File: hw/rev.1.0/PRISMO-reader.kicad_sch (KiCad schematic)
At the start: 48 parts, among them J1 Conn_01x03, J3 PN532 Connector, J4 External 5V power, J5 USB4120-03-C_REVA, K1 G5LE-1, Q1 2N7002, Q2 BC847, Q3 BC847, SW1 Logout button, U1 ESP32-WROOM-32D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

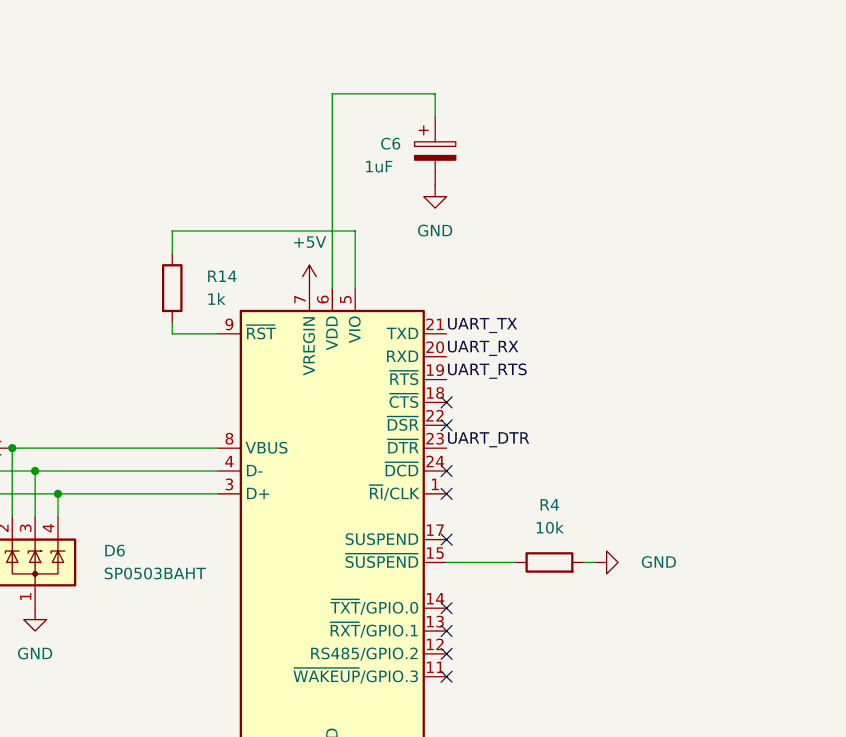
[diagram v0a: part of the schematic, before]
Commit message: fixed CP2102 peripheral connection
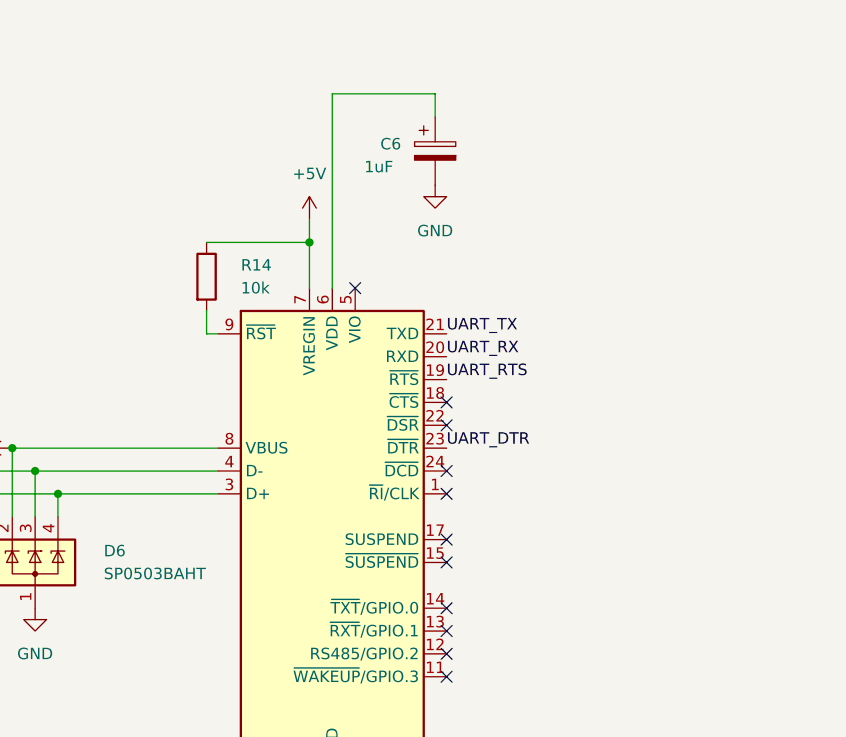
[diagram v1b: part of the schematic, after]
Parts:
- removed R4: 10k, Resistor_SMD:R_0805_2012Metric_Pad1.20x1.40mm_HandSolder, symbol Device:R
- R14: value 1k -> 10k
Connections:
- net +5V: now also R14.1
- net at U2.5 (VIO): no longer R14.1
- no-connect marks 28 -> 30
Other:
- moved on the sheet: R14

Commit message: renamed leds in order of connection
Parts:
- renumbered D3 to D1, D4 to D2, D2 to D3, D1 to D4
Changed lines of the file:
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@@
 		(dnp no)
 		(fields_autoplaced yes)
-		(property "Reference" "D3"
+		(property "Reference" "D1"
 			(at 45.72 39.532 0)
 			(effects
@@
 			(project "PRISMO-reader"
 				(path "/2a3560c2-ed74-4b68-8cf6-2c43628355c3"
-					(reference "D3")
+					(reference "D1")
 					(unit 1)
 				)
@@
 		(dnp no)
 		(fields_autoplaced yes)
-		(property "Reference" "D1"
+		(property "Reference" "D4"
 			(at 125.73 39.532 0)
 			(effects
@@
 			(project "PRISMO-reader"
 				(path "/2a3560c2-ed74-4b68-8cf6-2c43628355c3"
-					(reference "D1")
+					(reference "D4")
 					(unit 1)
 				)
@@
 		(dnp no)
 		(fields_autoplaced yes)
-		(property "Reference" "D4"
+		(property "Reference" "D2"
 			(at 68.58 39.532 0)
 			(effects
@@
 			(project "PRISMO-reader"
 				(path "/2a3560c2-ed74-4b68-8cf6-2c43628355c3"
-					(reference "D4")
+					(reference "D2")
 					(unit 1)
 				)
@@
 		(dnp no)
 		(fields_autoplaced yes)
-		(property "Reference" "D2"
+		(property "Reference" "D3"
 			(at 92.71 39.532 0)
 			(effects
@@
 			(project "PRISMO-reader"
 				(path "/2a3560c2-ed74-4b68-8cf6-2c43628355c3"
-					(reference "D2")
+					(reference "D3")
 					(unit 1)
 				)
